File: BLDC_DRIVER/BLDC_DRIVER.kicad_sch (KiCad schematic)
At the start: 0 parts

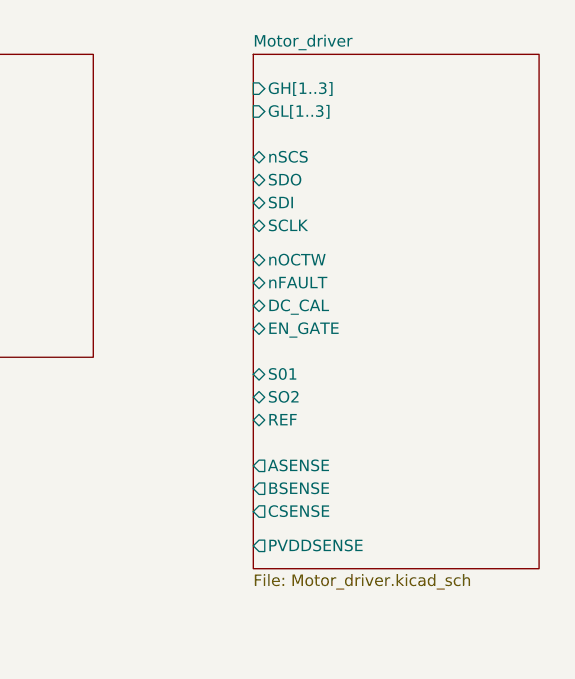
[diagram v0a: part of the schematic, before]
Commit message: BEMF measurement
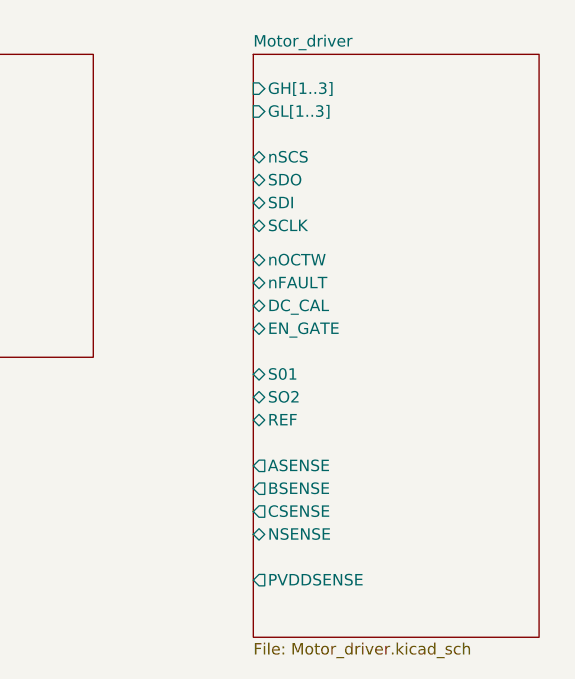
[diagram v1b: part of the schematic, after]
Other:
- sheet Motor_driver ports: added NSENSE; removed none
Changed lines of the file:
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@@
 	(sheet
 		(at 157.48 36.83)
-		(size 31.75 57.15)
+		(size 31.75 64.77)
 		(exclude_from_sim no)
 		(in_bom yes)
@@
 		)
 		(property "Sheetfile" "Motor_driver.kicad_sch"
-			(at 157.48 94.5646 0)
+			(at 157.48 102.1846 0)
 			(effects
 				(font
@@
 		)
 		(pin "PVDDSENSE" output
-			(at 157.48 91.44 180)
+			(at 157.48 95.25 180)
 			(effects
 				(font
+					(size 1.27 1.27)
+				)
+				(justify left)
+			)
+		)
+		(pin "NSENSE" bidirectional
+			(at 157.48 90.17 180)
+			(effects
+				(font

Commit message: new driver
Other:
- sheet Motor_driver ports: added CAL, ENABLE, NFAULT, NSCS, SensIA, SensIB, SensIC, SensVA, SensVB, SensVC, SensVN; removed ASENSE, BSENSE, CSENSE, DC_CAL, EN_GATE, NSENSE, REF, S01, SO2, nFAULT, nOCTW, nSCS
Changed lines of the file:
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@@
 			)
 		)
-		(pin "nFAULT" bidirectional
-			(at 157.48 62.23 180)
+		(pin "PVDDSENSE" output
+			(at 157.48 99.06 180)
 			(effects
 				(font
@@
 			)
 		)
-		(pin "SDO" bidirectional
-			(at 157.48 50.8 180)
+		(pin "SDO" input
+			(at 157.48 66.04 180)
 			(effects
 				(font
@@
 			)
 		)
-		(pin "REF" bidirectional
-			(at 157.48 77.47 180)
+		(pin "SCLK" input
+			(at 157.48 68.58 180)
 			(effects
 				(font
@@
 			)
 		)
-		(pin "nSCS" bidirectional
-			(at 157.48 48.26 180)
+		(pin "SensIA" input
+			(at 157.48 88.9 180)
 			(effects
 				(font
@@
 			)
 		)
-		(pin "nOCTW" bidirectional
-			(at 157.48 59.69 180)
+		(pin "ENABLE" input
+			(at 157.48 54.61 180)
 			(effects
 				(font
@@
 			)
 		)
-		(pin "SCLK" bidirectional
-			(at 157.48 55.88 180)
+		(pin "CAL" input
+			(at 157.48 52.07 180)
 			(effects
 				(font
@@
 			)
 		)
-		(pin "DC_CAL" bidirectional
-			(at 157.48 64.77 180)
+		(pin "SensVB" output
+			(at 157.48 81.28 180)
 			(effects
 				(font
@@
 			)
 		)
-		(pin "SDI" bidirectional
-			(at 157.48 53.34 180)
+		(pin "SensVC" output
+			(at 157.48 83.82 180)
 			(effects
 				(font
@@
 			)
 		)
-		(pin "EN_GATE" bidirectional
-			(at 157.48 67.31 180)
+		(pin "SensVA" output
+			(at 157.48 78.74 180)
 			(effects
 				(font
@@
 			)
 		)
-		(pin "BSENSE" output
-			(at 157.48 85.09 180)
+		(pin "SensVN" bidirectional
+			(at 157.48 76.2 180)
 			(effects
 				(font
@@
 			)
 		)
-		(pin "S01" bidirectional
-			(at 157.48 72.39 180)
+		(pin "NFAULT" input
+			(at 157.48 57.15 180)
 			(effects
 				(font
@@
 			)
 		)
-		(pin "ASENSE" output
-			(at 157.48 82.55 180)
+		(pin "SensIC" input
+			(at 157.48 93.98 180)
 			(effects
 				(font
@@
 			)
 		)
-		(pin "SO2" bidirectional
-			(at 157.48 74.93 180)
+		(pin "SensIB" input
+			(at 157.48 91.44 180)
 			(effects
 				(font
@@
 			)
 		)
-		(pin "CSENSE" output
-			(at 157.48 87.63 180)
+		(pin "NSCS" input
+			(at 157.48 71.12 180)
 			(effects
 				(font
@@
 			)
 		)
-		(pin "PVDDSENSE" output
-			(at 157.48 95.25 180)
+		(pin "SDI" input
+			(at 157.48 63.5 180)
 			(effects
 				(font
-					(size 1.27 1.27)
-				)
-				(justify left)
-			)
-		)
-		(pin "NSENSE" bidirectional
-			(at 157.48 90.17 180)
-			(effects
-				(font
